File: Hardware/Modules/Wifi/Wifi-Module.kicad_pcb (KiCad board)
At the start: 2 copper layers, 77 x 35 mm, 13 parts, among them J3 Conn_01x01_Pin, J4 B4B-EH-A, J5 Conn_01x10, J6 Conn_01x10, J7 B4B-EH-A, U1 ESP32-C6-MINI-1-H4, U2 TLV70033_SOT23-5

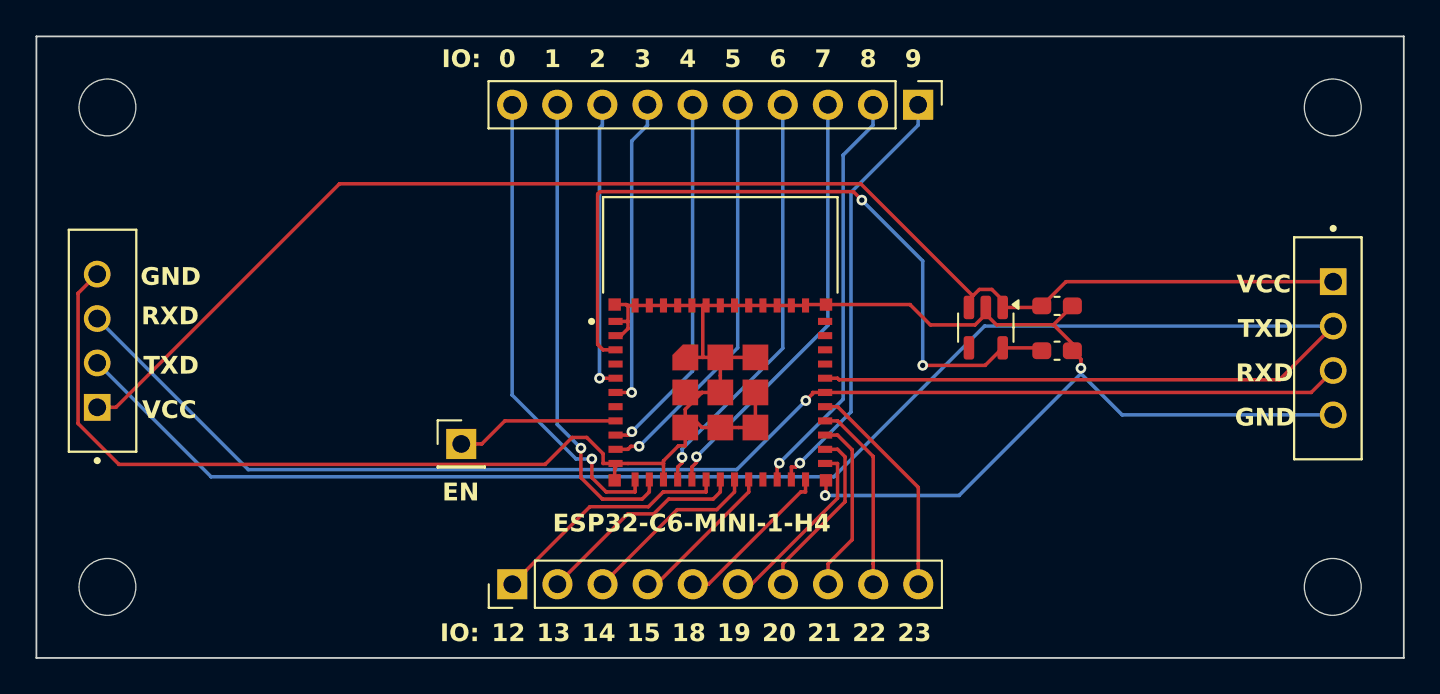
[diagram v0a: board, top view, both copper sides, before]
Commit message: Correction in the Wifi Module
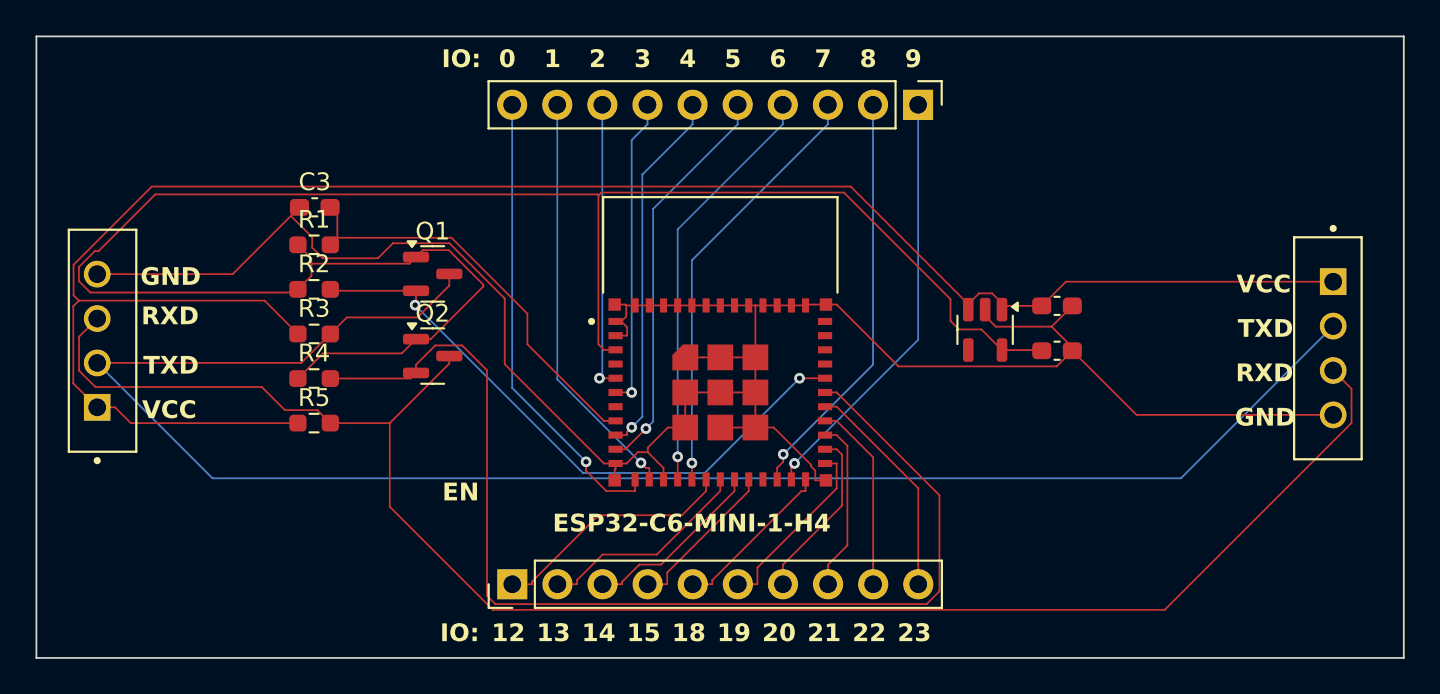
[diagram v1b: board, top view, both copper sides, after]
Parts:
- removed J3: Conn_01x01_Pin, Connector_PinHeader_2.54mm:PinHeader_1x01_P2.54mm_Vertical
- removed REF** (x4): MountingHole_3.2mm_M3, MountingHole:MountingHole_3.2mm_M3
- added C3: 1µ, Capacitor_SMD:C_0603_1608Metric_Pad1.08x0.95mm_HandSolder, F.Cu at (116.1, 114.5)
- added Q1: BSS138, Package_TO_SOT_SMD:SOT-23, F.Cu at (122.7, 118.2)
- added Q2: BSS138, Package_TO_SOT_SMD:SOT-23, F.Cu at (122.7, 122.9)
- added R1: 10k, Resistor_SMD:R_0603_1608Metric_Pad0.98x0.95mm_HandSolder, F.Cu at (116.1, 116.6)
- added R2: 10k, Resistor_SMD:R_0603_1608Metric_Pad0.98x0.95mm_HandSolder, F.Cu at (116.1, 119.1)
- added R3: 10k, Resistor_SMD:R_0603_1608Metric_Pad0.98x0.95mm_HandSolder, F.Cu at (116.1, 121.6)
- added R4: 10k, Resistor_SMD:R_0603_1608Metric_Pad0.98x0.95mm_HandSolder, F.Cu at (116.1, 124.1)
- added R5: 10k, Resistor_SMD:R_0603_1608Metric_Pad0.98x0.95mm_HandSolder, F.Cu at (116.1, 126.7)
- moved U2 0.13 mm to (153.8, 121.4)
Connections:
- J4 pad 2: TXD -> H_TXD
- J4 pad 3: RXD -> H_RXD
- J7 pad 2: TXD -> H_TXD
- J7 pad 3: RXD -> H_RXD
- U1 pad 30: RXD -> L_RXD
- U1 pad 31: TXD -> L_TXD
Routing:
- net TXD: track 105.7 -> 0.00 mm
- net H_TXD: track 0.00 -> 98.1 mm
- net H_RXD: track 0.00 -> 96.3 mm
- net RXD: track 75.5 -> 0.00 mm, vias 1 -> 0
- net 3V3: track 42.6 -> 110.0 mm, vias 2 -> 0
- net L_RXD: track 0.00 -> 63.4 mm
- net L_TXD: track 0.00 -> 34.9 mm, vias 0 -> 2
- net Vcc: track 79.6 -> 110.8 mm
- net Net-(U1-EN): track 9.23 -> 23.4 mm
- net GND: track 135.4 -> 126.9 mm, vias 2 -> 0
- net Net-(J5-Pin_9): track 26.8 -> 23.4 mm
- net Net-(J5-Pin_10): track 26.8 -> 26.2 mm

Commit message: Forgot the ground surfaces
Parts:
- added REF**: MountingHole_3.2mm_M3, MountingHole:MountingHole_3.2mm_M3, F.Cu at (104.4, 135.9)
- added REF**: MountingHole_3.2mm_M3, MountingHole:MountingHole_3.2mm_M3, F.Cu at (104.4, 108.9)
- added REF**: MountingHole_3.2mm_M3, MountingHole:MountingHole_3.2mm_M3, F.Cu at (173.4, 108.9)
- added REF**: MountingHole_3.2mm_M3, MountingHole:MountingHole_3.2mm_M3, F.Cu at (173.4, 135.9)
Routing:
- added copper zone on B.Cu, net GND
- added copper zone on F.Cu, net GND

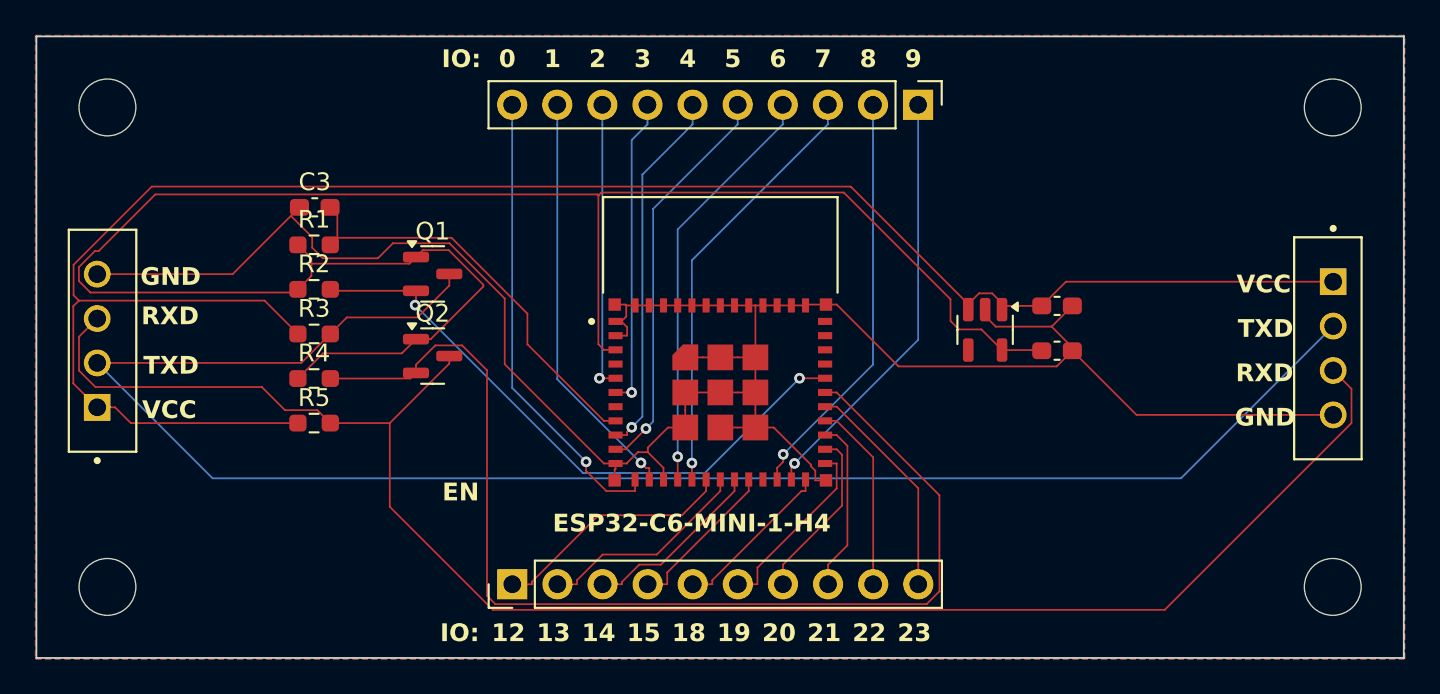
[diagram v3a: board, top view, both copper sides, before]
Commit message: Finall Version of the Wifi-Module (correct mistakes))
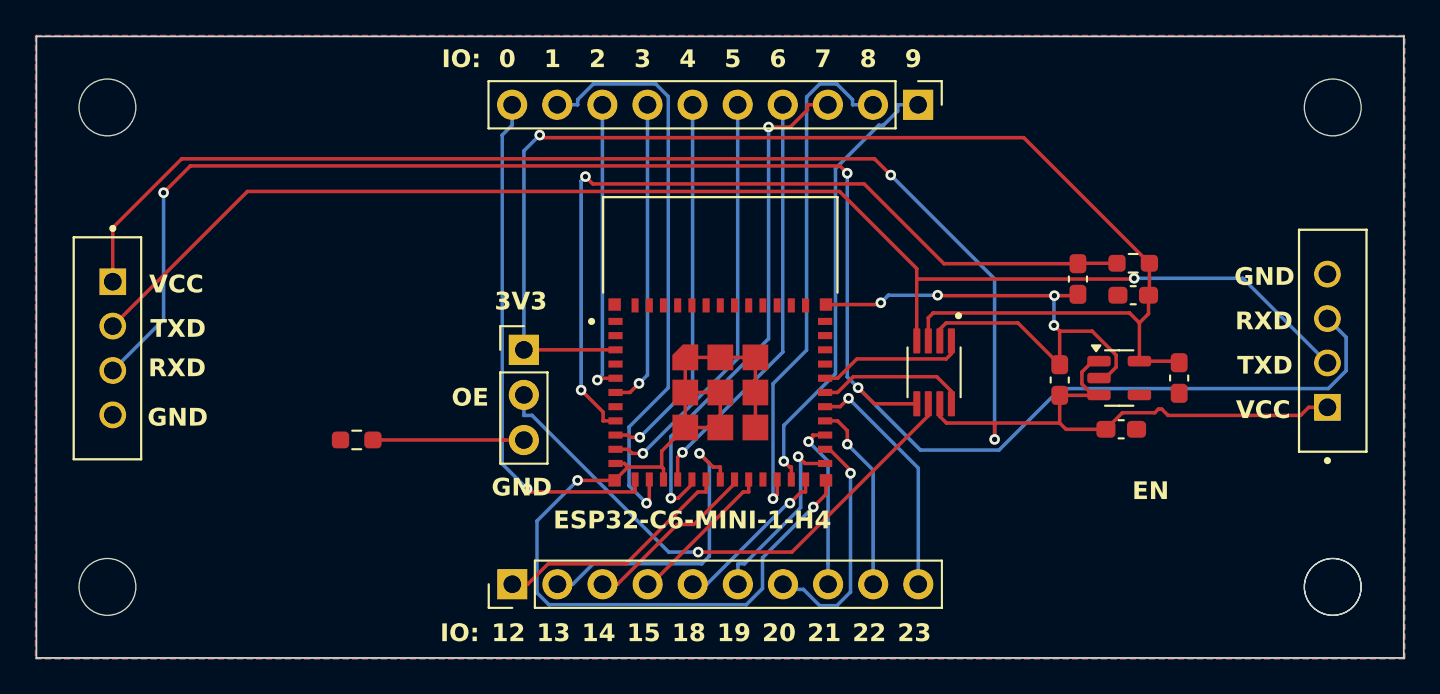
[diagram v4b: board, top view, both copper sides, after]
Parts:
- removed Q1, Q2: BSS138, Package_TO_SOT_SMD:SOT-23
- removed R3, R4, R5: 10k, Resistor_SMD:R_0603_1608Metric_Pad0.98x0.95mm_HandSolder
- added ?: , , F.Cu at (173.4, 135.9)
- added C4: 0.1µF, Capacitor_SMD:C_0603_1608Metric_Pad1.08x0.95mm_HandSolder, F.Cu at (162.2, 119.5)
- added C5: 0.1µF, Capacitor_SMD:C_0603_1608Metric_Pad1.08x0.95mm_HandSolder, F.Cu at (158.1, 124.2)
- added J1: Conn_01x03_Pin, Connector_PinHeader_2.54mm:PinHeader_1x03_P2.54mm_Vertical, F.Cu at (127.9, 122.5)
- added U3: TXS0102DCTR, Modular-Elektronics-Toolkit-Global-Libary:TXS0102DCTR, F.Cu at (151.0, 123.8)
- J4, J7: footprint Modular-Electronics-Toolkit-BP:JST_B4B-EH-A -> Modular-Elektronics-Toolkit-Global-Libary:JST_B4B-EH-A
- U1: footprint Modular-Electronics-Toolkit-BP:XCVR_ESP32-C6-MINI-1-H4 -> Modular-Elektronics-Toolkit-Global-Libary:XCVR_ESP32-C6-MINI-1-H4
- moved R1 46.1 mm to (162.2, 117.7), turned to 180 degrees
- moved C3 43.2 mm to (159.1, 118.5), turned to 90 degrees
- moved R2 8.81 mm to (118.5, 127.6)
- moved U2 8.02 mm to (161.4, 124.1), turned to 0 degrees
- moved C1 7.83 mm to (161.5, 127.0)
- moved C2 7.04 mm to (164.8, 124.1), turned to -90 degrees
- moved J4 0.97 mm to (104.7, 122.4), turned to -90 degrees
- moved J7 0.54 mm to (173.1, 122.0), turned to 90 degrees
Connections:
- R2 pad 1: 3V3 -> GND
- R2 pad 2: L_TXD -> Net-(J1-Pin_3)
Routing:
- net L_RXD: track 63.4 -> 8.52 mm
- net GND: track 126.9 -> 88.0 mm, vias 0 -> 6
- net 3V3: track 110.0 -> 76.5 mm, vias 0 -> 1
- net Net-(J1-Pin_2): track 0.00 -> 31.0 mm, vias 0 -> 1
- net L_TXD: track 34.9 -> 8.41 mm, vias 2 -> 0
- net Net-(U1-EN): track 23.4 -> 47.0 mm, vias 0 -> 2
- net H_TXD: track 98.1 -> 79.4 mm, vias 0 -> 1
- net Vcc: track 110.8 -> 97.6 mm, vias 0 -> 2
- net Net-(J5-Pin_9): track 23.4 -> 32.8 mm
- net Net-(J1-Pin_3): track 0.00 -> 8.50 mm
- net Net-(J5-Pin_2): track 23.3 -> 29.3 mm
- net Net-(J6-Pin_2): track 12.1 -> 17.4 mm, vias 0 -> 1
- net Net-(J5-Pin_3): track 24.3 -> 29.0 mm, vias 1 -> 2
- net H_RXD: track 96.3 -> 100.7 mm, vias 0 -> 3
- net Net-(J6-Pin_7): track 9.75 -> 13.4 mm, vias 0 -> 1
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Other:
- board text added: "3V3"
- board text added: "OE"
